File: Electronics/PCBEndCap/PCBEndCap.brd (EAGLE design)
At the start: 63.5 x 31.8 mm, 2 parts, among them J1 CONNECTOR_8PIN, J2 CONNECTOR_8PIN

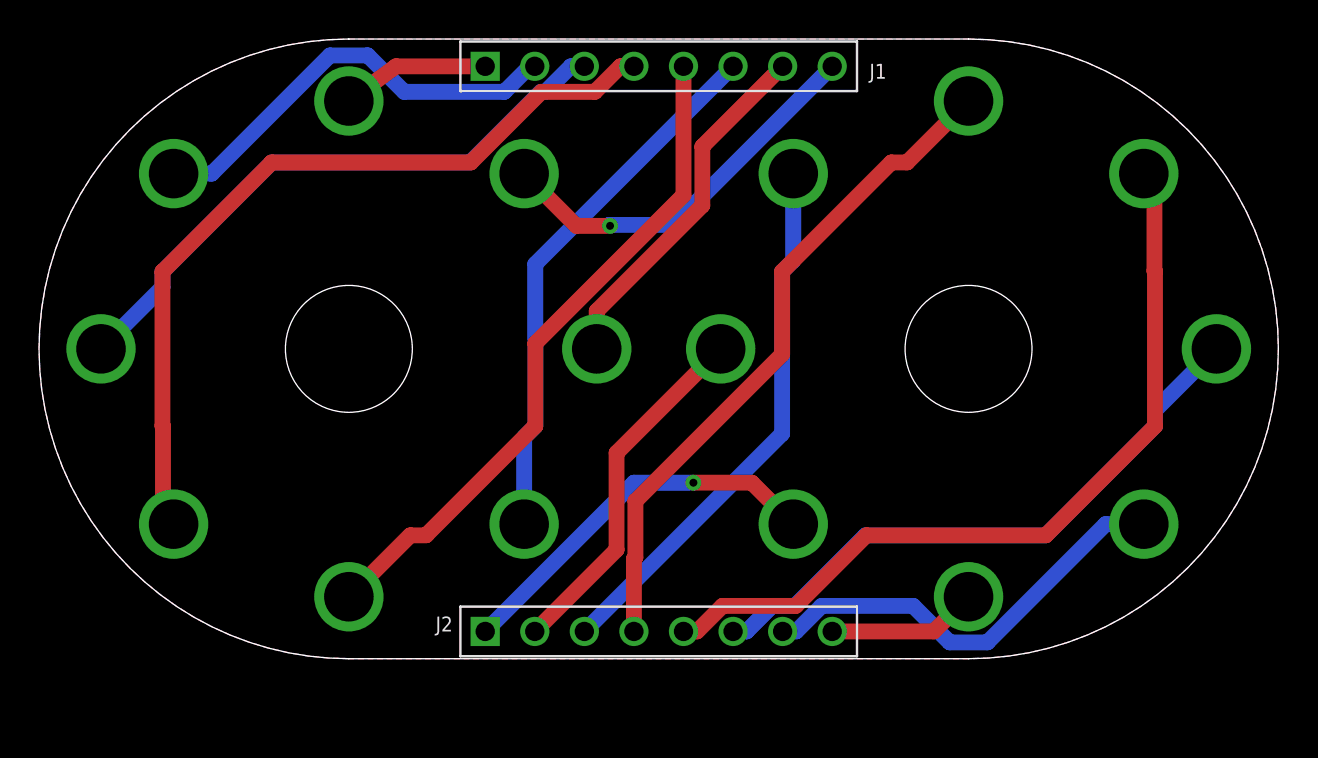
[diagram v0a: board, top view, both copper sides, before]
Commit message: redesigned PCBEndCap to include GND and VCC
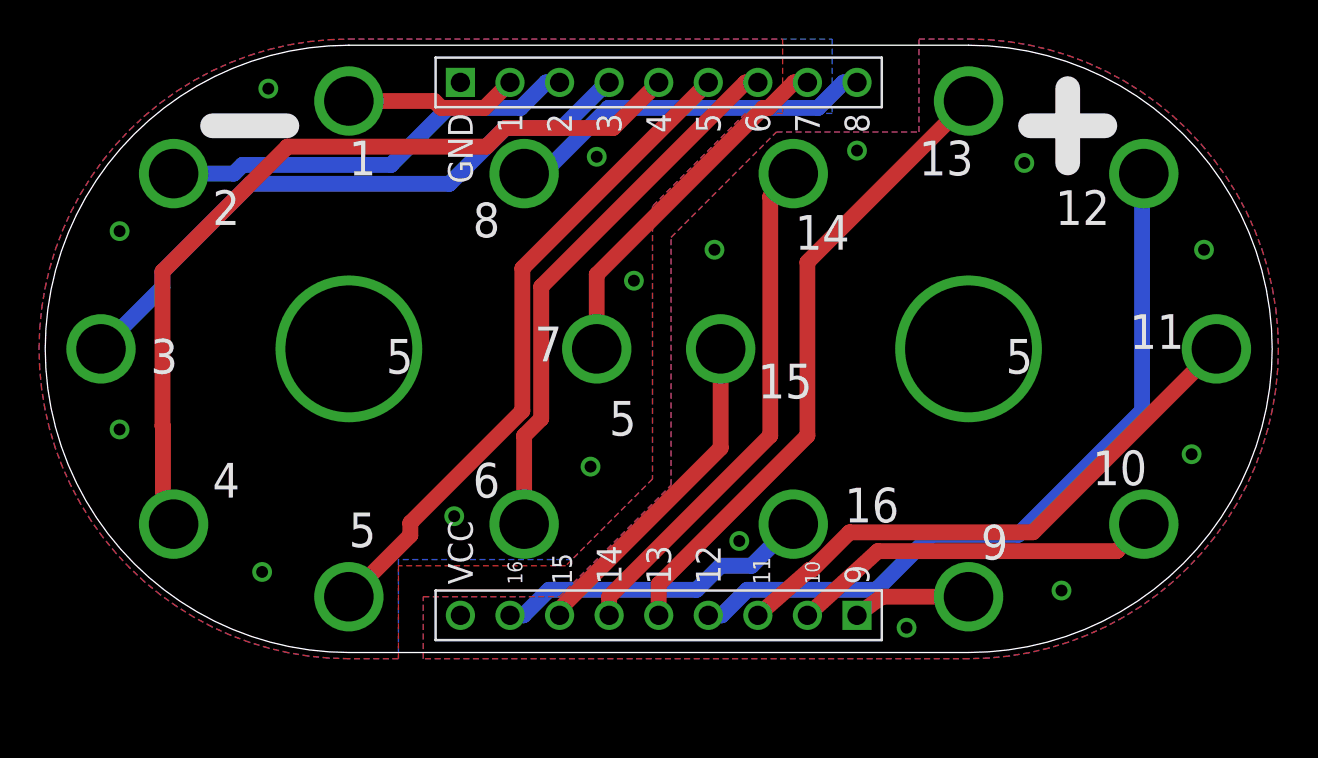
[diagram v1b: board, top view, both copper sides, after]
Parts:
- removed J1, J2: CONNECTOR_8PIN, lolomolo:8PIN_.1'
- added J3, J4: CONNECTOR_9PIN, lolomolo:9PIN_.1'
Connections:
- new net GND: J3.1
- new net VCC: J4.9
- net N1: now also J3.2; no longer J1.P$1
- net N10: now also J4.2; no longer J2.P$2
- net N11: now also J4.3; no longer J2.P$3
- net N12: now also J4.4; no longer J2.P$4
- net N13: now also J4.5; no longer J2.P$5
- net N14: now also J4.6; no longer J2.P$6
- net N15: now also J4.7; no longer J2.P$7
- net N16: now also J4.8; no longer J2.P$8
- net N2: now also J3.3; no longer J1.P$2
- net N3: now also J3.4; no longer J1.P$3
- net N4: now also J3.5; no longer J1.P$4
- net N5: now also J3.6; no longer J1.P$5
- net N6: now also J3.7; no longer J1.P$6
- net N7: now also J3.8; no longer J1.P$7
- net N8: now also J3.9; no longer J1.P$8
- net N9: now also J4.1; no longer J2.P$1
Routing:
- net N9: track 19.8 -> 6.03 mm, vias 2 -> 1
- net N13: track 41.7 -> 32.9 mm
- net N16: track 7.72 -> 16.5 mm
- net N15: track 22.3 -> 17.1 mm
- net N14: track 31.2 -> 26.5 mm
- net N12: track 34.8 -> 38.8 mm
- net N8: track 20.4 -> 19.0 mm, vias 2 -> 1
- net N1: track 7.57 -> 8.94 mm
- net N11: track 27.9 -> 29.1 mm
- net N4: track 41.7 -> 42.6 mm
- net N3: track 31.2 -> 32.2 mm
- net N5: track 34.8 -> 34.0 mm
- net N10: track 18.4 -> 19.1 mm
- net N2: track 22.3 -> 21.7 mm
- added copper zone on layer 1, net GND
- added copper zone on layer 16, net GND
- added copper zone on layer 1, net VCC
- added copper zone on layer 16, net VCC
- removed copper zone on layer 16, net N$1
- removed copper zone on layer 1, net N$4
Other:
- board size 63.5 x 31.8 mm -> 62.9 x 31.1 mm
- board text added: "1"
- board text added: "10"
- board text added: "11"
- board text added: "12"
- board text added: "13"
- board text added: "14"
- board text added: "15"
- board text added: "16"
- board text added: "2"
- board text added: "3"
- board text added: "4"
- board text added: "5"
- board text added: "6"
- board text added: "7"
- board text added: "8"
- board text added: "9"
- board text added: "GND"
- board text added: "VCC"

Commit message: pcb spacer and breakoutoard over
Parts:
- removed J3, J4: CONNECTOR_9PIN, lolomolo:9PIN_.1'
- added J1: CONNECTORJST2X9_2MM, MarkIIEaglelbr:CONNECTOR9X2_2MMPITCH
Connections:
- removed net N1: J3.2
- removed net N10: J4.2
- removed net N11: J4.3
- removed net N12: J4.4
- removed net N13: J4.5
- removed net N14: J4.6
- removed net N15: J4.7
- removed net N16: J4.8
- removed net N2: J3.3
- removed net N3: J3.4
- removed net N4: J3.5
- removed net N5: J3.6
- removed net N6: J3.7
- removed net N7: J3.8
- removed net N8: J3.9
- removed net N9: J4.1
- new net B1: J1.P$2
- new net B10: J1.P$7
- new net B11: J1.P$6
- new net B12: J1.P$14
- new net B13: J1.P$13
- new net B14: J1.P$12
- new net B15: J1.P$11
- new net B16: J1.P$10
- new net B2: J1.P$3
- new net B3: J1.P$4
- new net B4: J1.P$5
- new net B5: J1.P$15
- new net B6: J1.P$16
- new net B7: J1.P$17
- new net B8: J1.P$18
- new net B9: J1.P$8
- net GND: now also J1.P$1; no longer J3.1
- net VCC: now also J1.P$9; no longer J4.9
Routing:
- net B12: track 0.00 -> 46.3 mm, vias 0 -> 1
- net B4: track 0.00 -> 42.9 mm, vias 0 -> 2
- net N4: track 42.6 -> 0.00 mm, vias 1 -> 0
- net N12: track 38.8 -> 0.00 mm, vias 1 -> 0
- net B3: track 0.00 -> 35.4 mm, vias 0 -> 1
- net B11: track 0.00 -> 34.7 mm, vias 0 -> 2
- net N5: track 34.0 -> 0.00 mm, vias 1 -> 0
- net B5: track 0.00 -> 33.9 mm, vias 0 -> 1
- net B13: track 0.00 -> 33.2 mm, vias 0 -> 1
- net N13: track 32.9 -> 0.00 mm, vias 1 -> 0
- net N3: track 32.2 -> 0.00 mm, vias 1 -> 0
- net N11: track 29.1 -> 0.00 mm, vias 1 -> 0
- net B6: track 0.00 -> 28.4 mm, vias 0 -> 1
- net N6: track 28.0 -> 0.00 mm, vias 1 -> 0
- net N14: track 26.5 -> 0.00 mm, vias 1 -> 0
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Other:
- board size 62.9 x 31.1 mm -> 62.2 x 30.5 mm
- board text removed: "GND"
- board text removed: "VCC"
